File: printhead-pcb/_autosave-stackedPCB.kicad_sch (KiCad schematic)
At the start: 11 parts, among them J13 Steckverbinder_Male_1, J14 Steckverbinder_Male_2, J15 Steckverbinder_Female_2

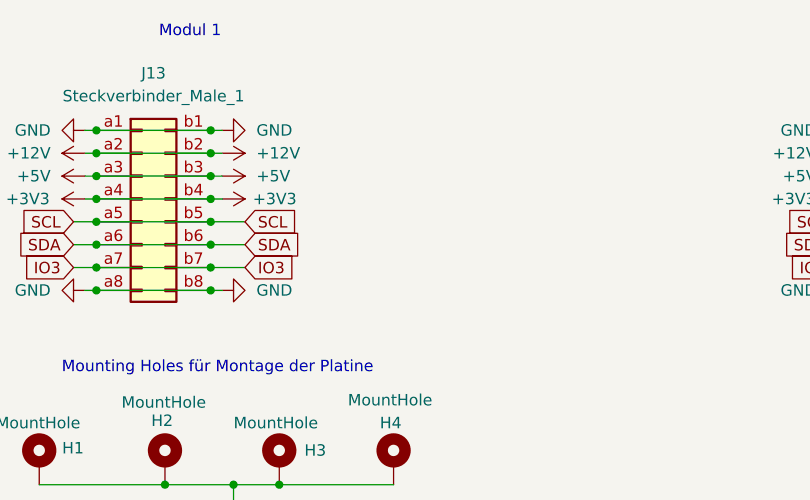
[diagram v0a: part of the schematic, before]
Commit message: layed out all tracks and played around more with net classes
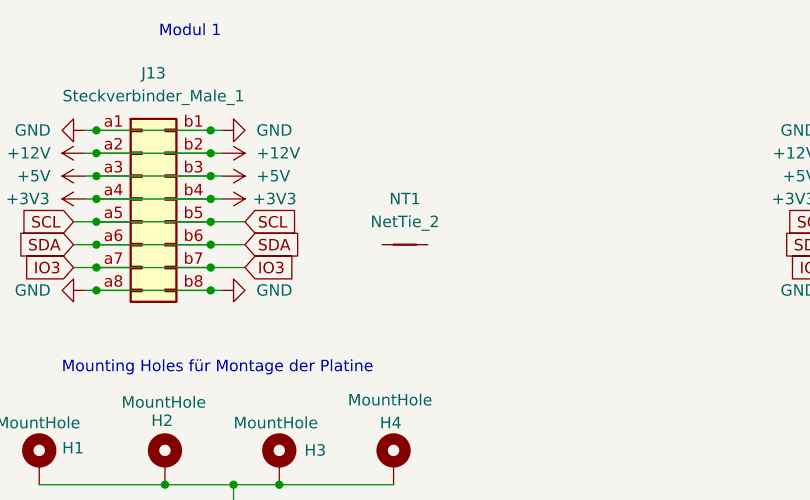
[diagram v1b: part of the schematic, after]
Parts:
- added NT1: NetTie_2, symbol Device:NetTie_2
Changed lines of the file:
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@@
+	)
+	(symbol
+		(lib_id "Device:NetTie_2")
+		(at 64.77 40.64 0)
+		(unit 1)
+		(exclude_from_sim no)
+		(in_bom no)
+		(on_board yes)
+		(dnp no)
+		(fields_autoplaced yes)
+		(property "Reference" "NT1"
+			(at 64.77 35.56 0)
+			(effects
+				(font
+					(size 1.27 1.27)
+				)
+			)
+		)
+		(property "Value" "NetTie_2"
+			(at 64.77 38.1 0)
+			(effects
+				(font
+					(size 1.27 1.27)
+				)
+			)
+		)
+		(property "Footprint" ""
+			(at 64.77 40.64 0)
+			(effects
+				(font
+					(size 1.27 1.27)
+				)
+				(hide yes)
+			)
+		)
+		(property "Datasheet" "~"
+			(at 64.77 40.64 0)
+			(effects
+				(font
+					(size 1.27 1.27)
+				)
+				(hide yes)
+			)
+		)
+		(property "Description" "Net tie, 2 pins"
+			(at 64.77 40.64 0)
+			(effects
+				(font
+					(size 1.27 1.27)
+				)
+				(hide yes)
+			)
+		)
+		(pin "2"
+		)
+		(pin "1"
+		)
+		(instances
+			(project ""
+				(path "/813ad687-b864-44a5-b729-c4edf26b731d/973cbd04-4685-459c-b508-5e140dd5518f"
+					(reference "NT1")
+					(unit 1)
+				)
+			)
+		)
 	)
 	(symbol
